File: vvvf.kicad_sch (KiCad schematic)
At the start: 14 parts, among them Q1 Q_NIGBT_GCE, Q2 Q_NIGBT_GCE, U1 TLP152, U2 TLP152

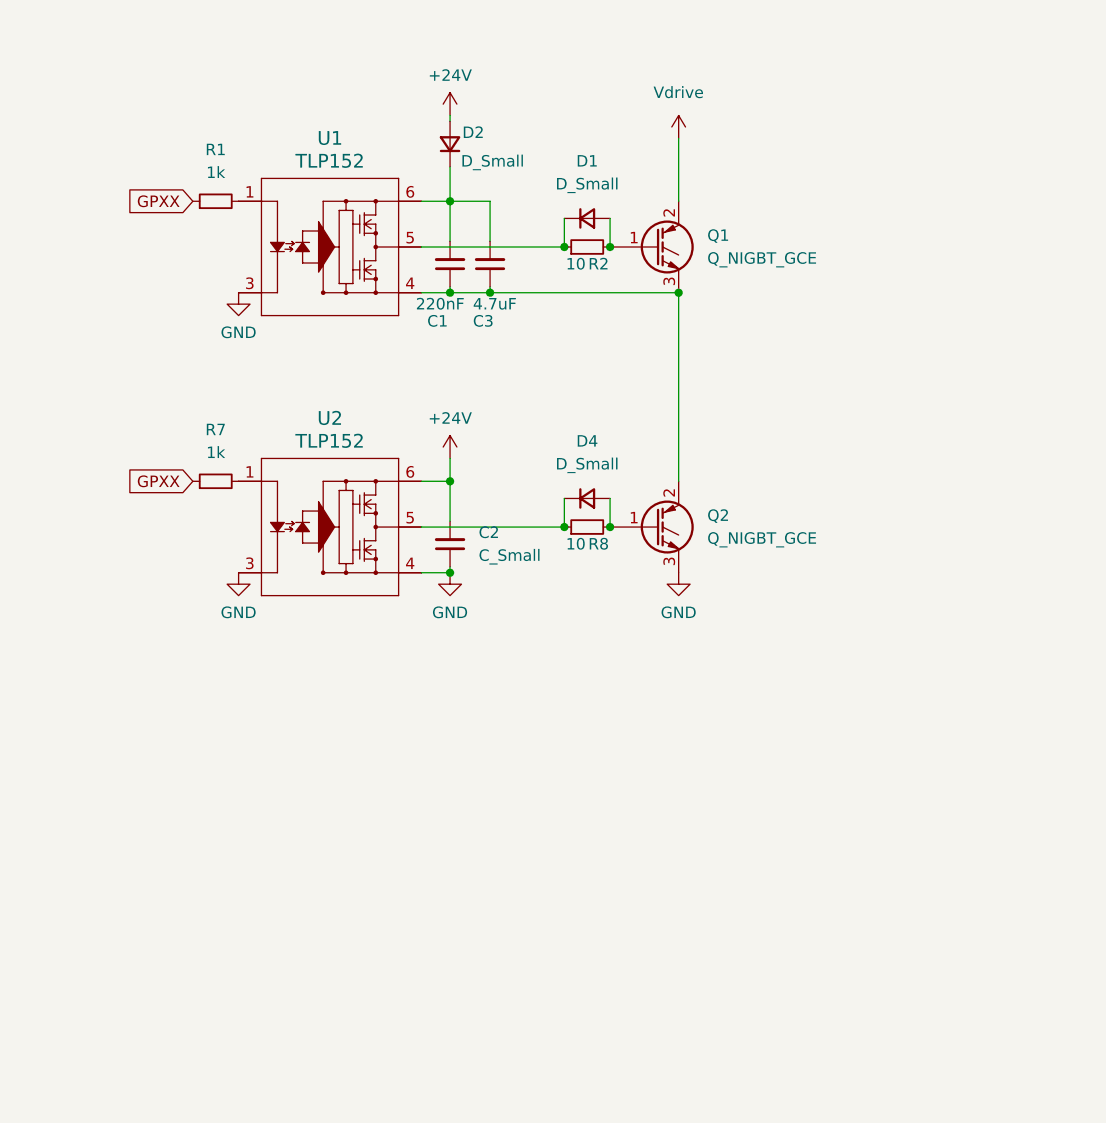
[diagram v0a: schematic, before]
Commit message: push to github so i can keep editing journal on web editor
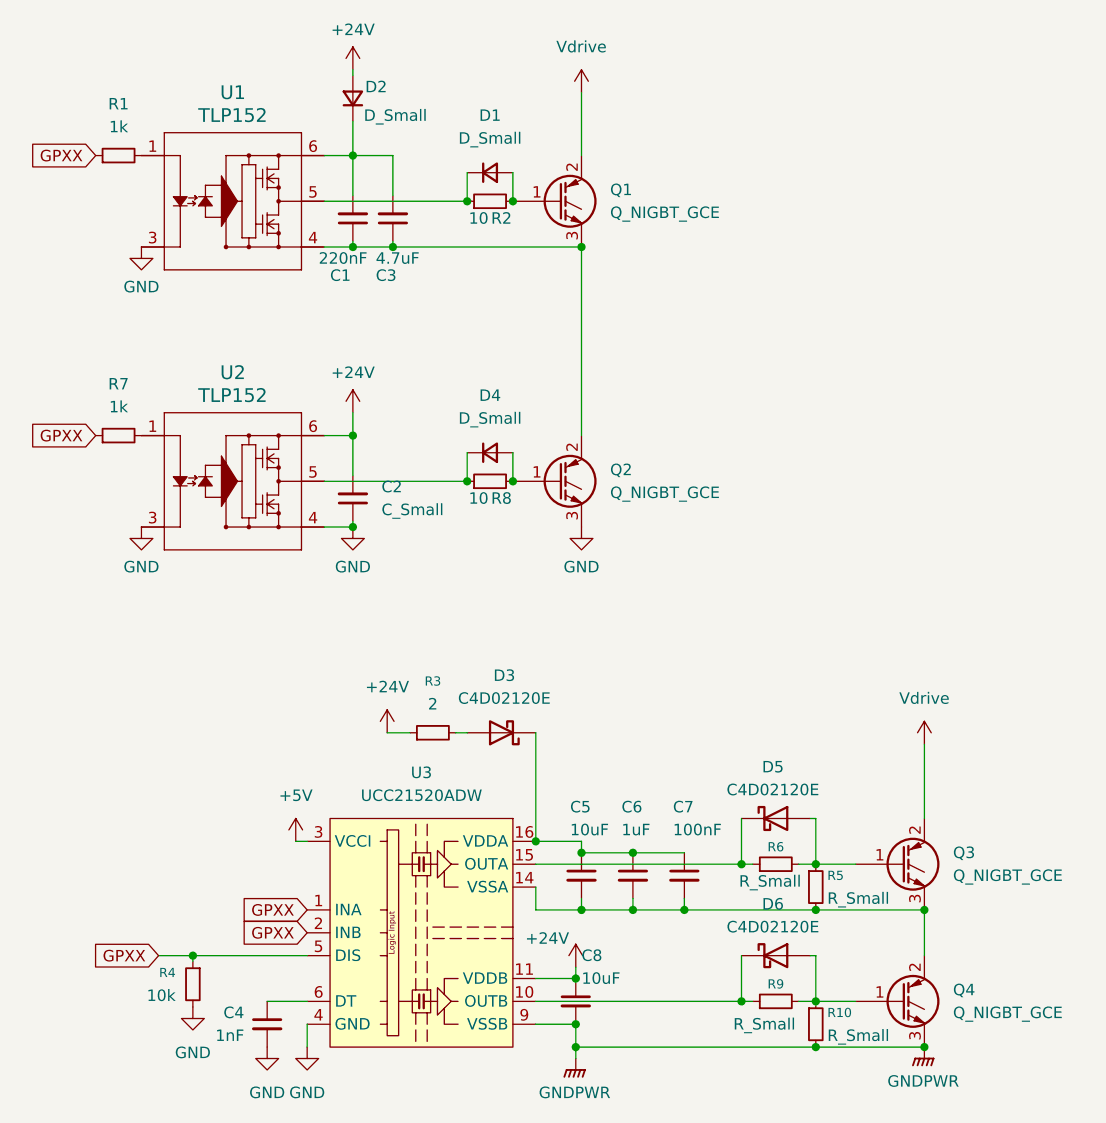
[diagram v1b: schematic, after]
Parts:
- added C4: 1nF, symbol Device:C_Small
- added C5, C8: 10uF, symbol Device:C_Small
- added C6: 1uF, symbol Device:C_Small
- added C7: 100nF, symbol Device:C_Small
- added D3, D5, D6: C4D02120E, Package_TO_SOT_SMD:TO-252-2_TabPin1, symbol Diode:C4D02120E
- added Q3, Q4: Q_NIGBT_GCE, symbol Device:Q_NIGBT_GCE
- added R10, R5, R6, R9: R_Small, symbol Device:R_Small
- added R3: 2, symbol Device:R_Small
- added R4: 10k, symbol Device:R_Small
- added U3: UCC21520ADW, Package_SO:SOIC-16W_7.5x10.3mm_P1.27mm, symbol Driver_FET:UCC21520ADW
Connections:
- net +24V: now also C8.1, R3.1, U3.11 (VDDB)
- net GND: now also C4.2, R4.2, U3.4 (GND)
- net GPXX: now also R4.1, U3.1 (INA), U3.2 (INB), U3.5 (DIS)
- net Vdrive: now also Q3.2 (C)
- new net: D5.2 (A), Q3.1 (G), R5.1, R6.2
- new net: C5.2, C6.2, C7.2, Q3.3 (E), Q4.2 (C), R5.2, U3.14 (VSSA)
- new net: D6.2 (A), Q4.1 (G), R10.1, R9.2
- new net: C5.1, C6.1, C7.1, D3.1 (K), U3.16 (VDDA)
- new net: D3.2 (A), R3.2
- new net: D6.1 (K), R9.1, U3.10 (OUTB)
- new net: D5.1 (K), R6.1, U3.15 (OUTA)
- new net: C4.1, U3.6 (DT)
- new net +5V: U3.3 (VCCI), U3.8 (VCCI)
- new net GNDPWR: C8.2, Q4.3 (E), R10.2, U3.9 (VSSB)
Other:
- moved on the sheet: C1, C2, C3, D1, D2, D4, Q1, Q2, R1, R2, R7, R8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
